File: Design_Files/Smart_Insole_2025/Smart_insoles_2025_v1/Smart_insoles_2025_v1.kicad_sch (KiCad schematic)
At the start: 9 parts, among them J1 Conn_01x20, U1 ESP32-C3_SUPERMINI_SMD, U2 CD74HC4067M96

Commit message: updated Schematic & PCB layout
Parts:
- added C2, C3: C, Capacitor_SMD:C_0603_1608Metric_Pad1.08x0.95mm_HandSolder, symbol Device:C
- added J2: Conn_01x02_Pin, Connector_JST:JST_EH_S2B-EH_1x02_P2.50mm_Horizontal, symbol Connector:Conn_01x02_Pin
- RN1, RN2: value R_Pack04 -> 10k
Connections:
- net +BATT: now also J2.2 (Pin_2)
- net -BATT: now also J2.1 (Pin_1)
- net GND: now also C2.2, C3.2
- net VCC: now also C2.1, C3.1
- no-connect marks 19 -> 20
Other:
- note added: "Decoupling Capacitors"
- note added: "MCU"

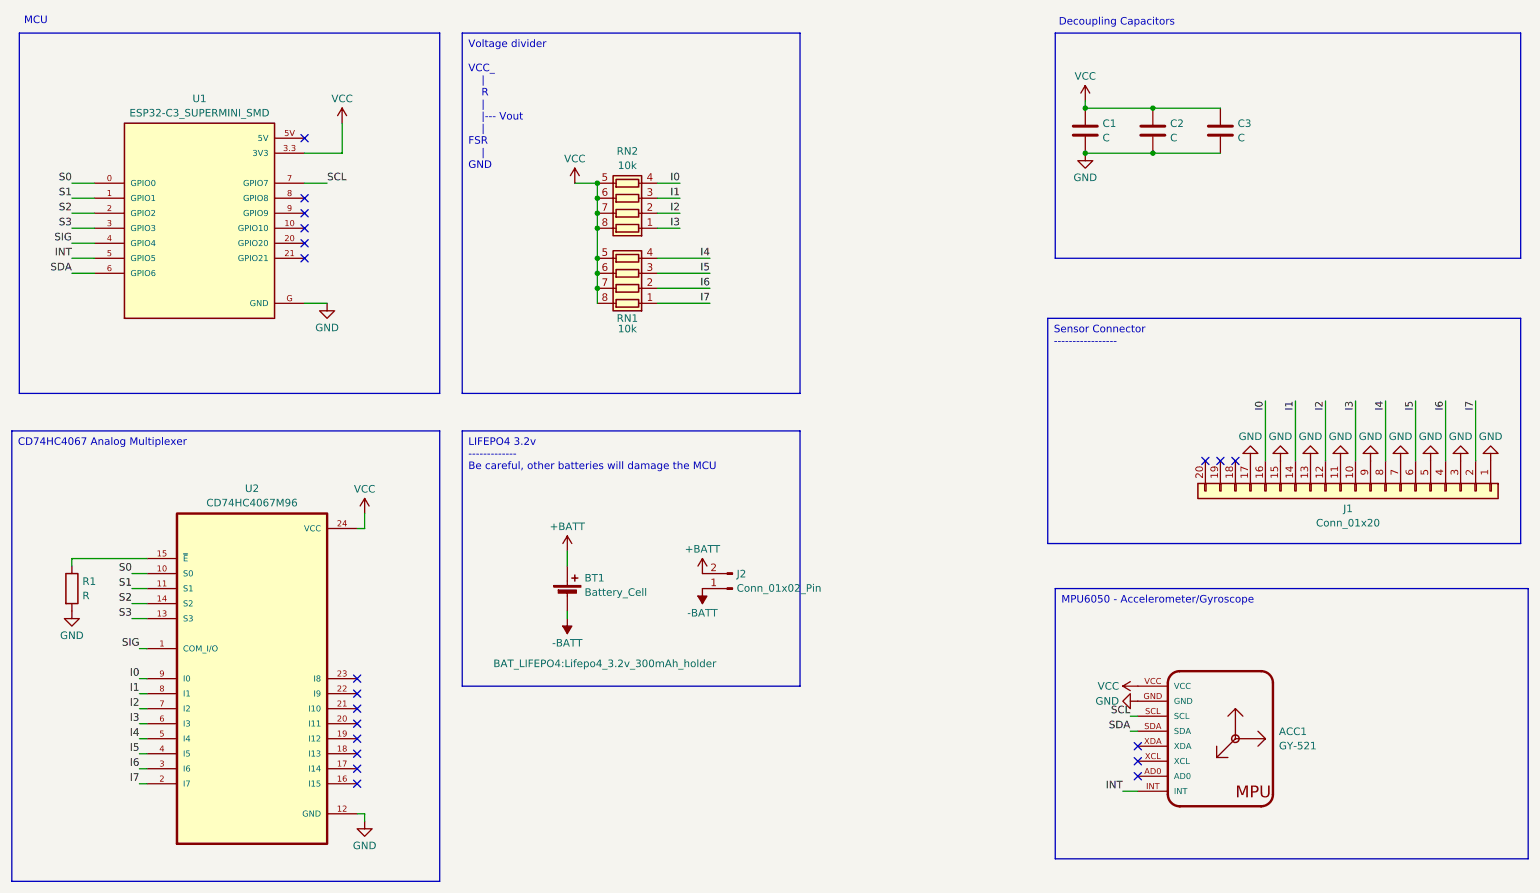
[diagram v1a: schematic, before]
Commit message: Added AFE from mikroe clicker schematic. Reorganized Schematic in general
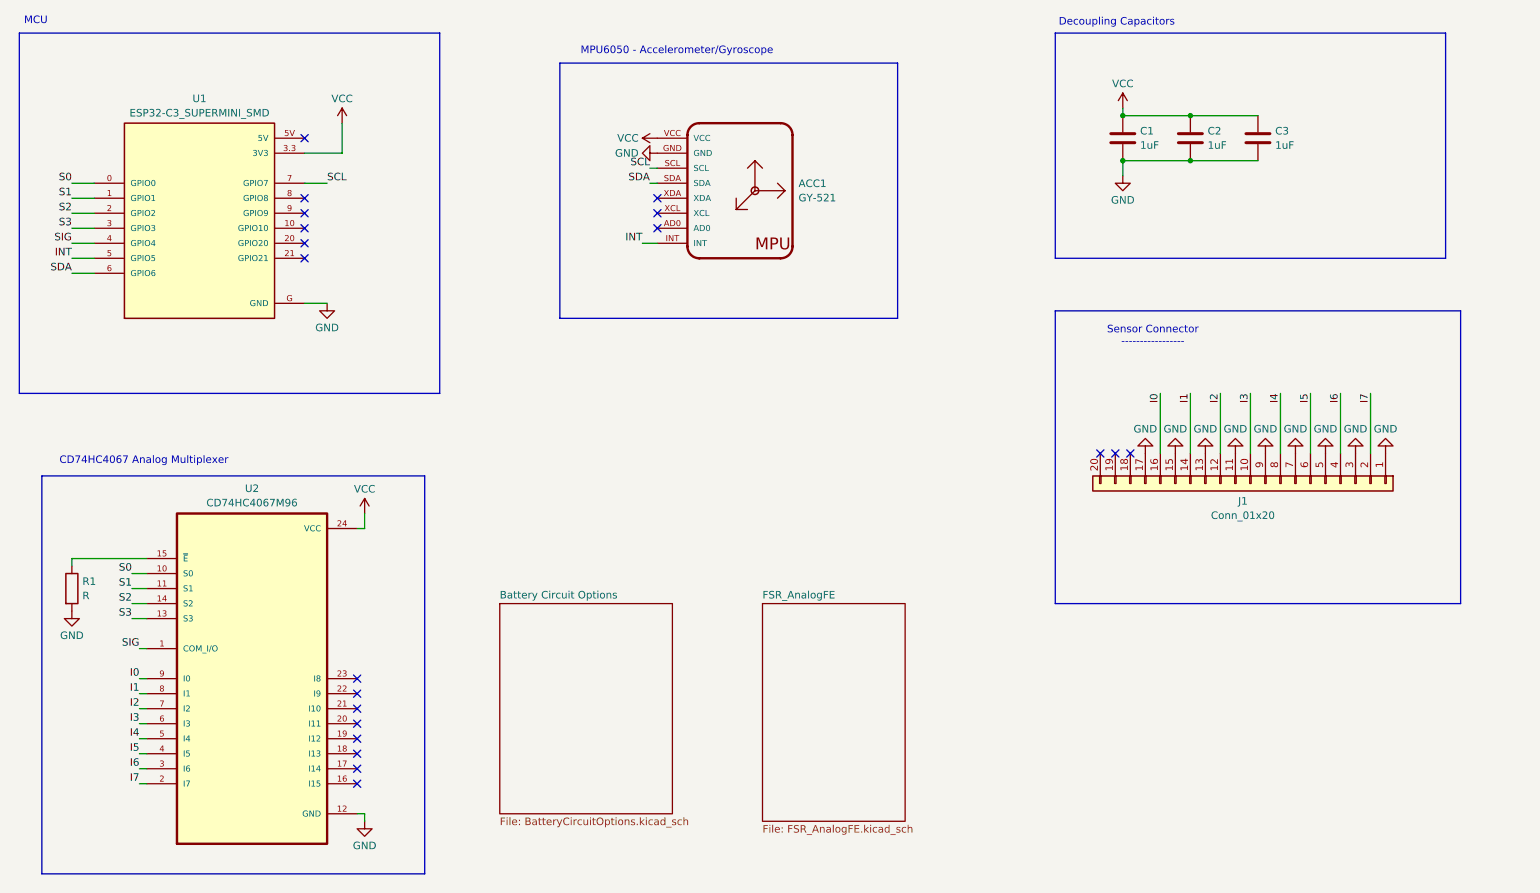
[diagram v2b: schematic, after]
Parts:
- removed BT1: Battery_Cell, BAT_LIFEPO4:Lifepo4_3.2v_300mAh_holder, symbol Device:Battery_Cell
- removed J2: Conn_01x02_Pin, Connector_JST:JST_EH_S2B-EH_1x02_P2.50mm_Horizontal, symbol Connector:Conn_01x02_Pin
- removed RN1, RN2: 10k, Resistor_SMD:R_Array_Concave_4x0603, symbol Device:R_Pack04
- C1, C2, C3: value C -> 1uF
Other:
- added sheet Battery Circuit Options (BatteryCircuitOptions.kicad_sch)
- added sheet FSR_AnalogFE (FSR_AnalogFE.kicad_sch)
- note added: "CD74HC4067 Analog Multiplexer"
- note added: "MPU6050 - Accelerometer/Gyroscope"
- note added: "Sensor Connector -----------------"
- moved on the sheet: ACC1, C1, C2, C3, J1

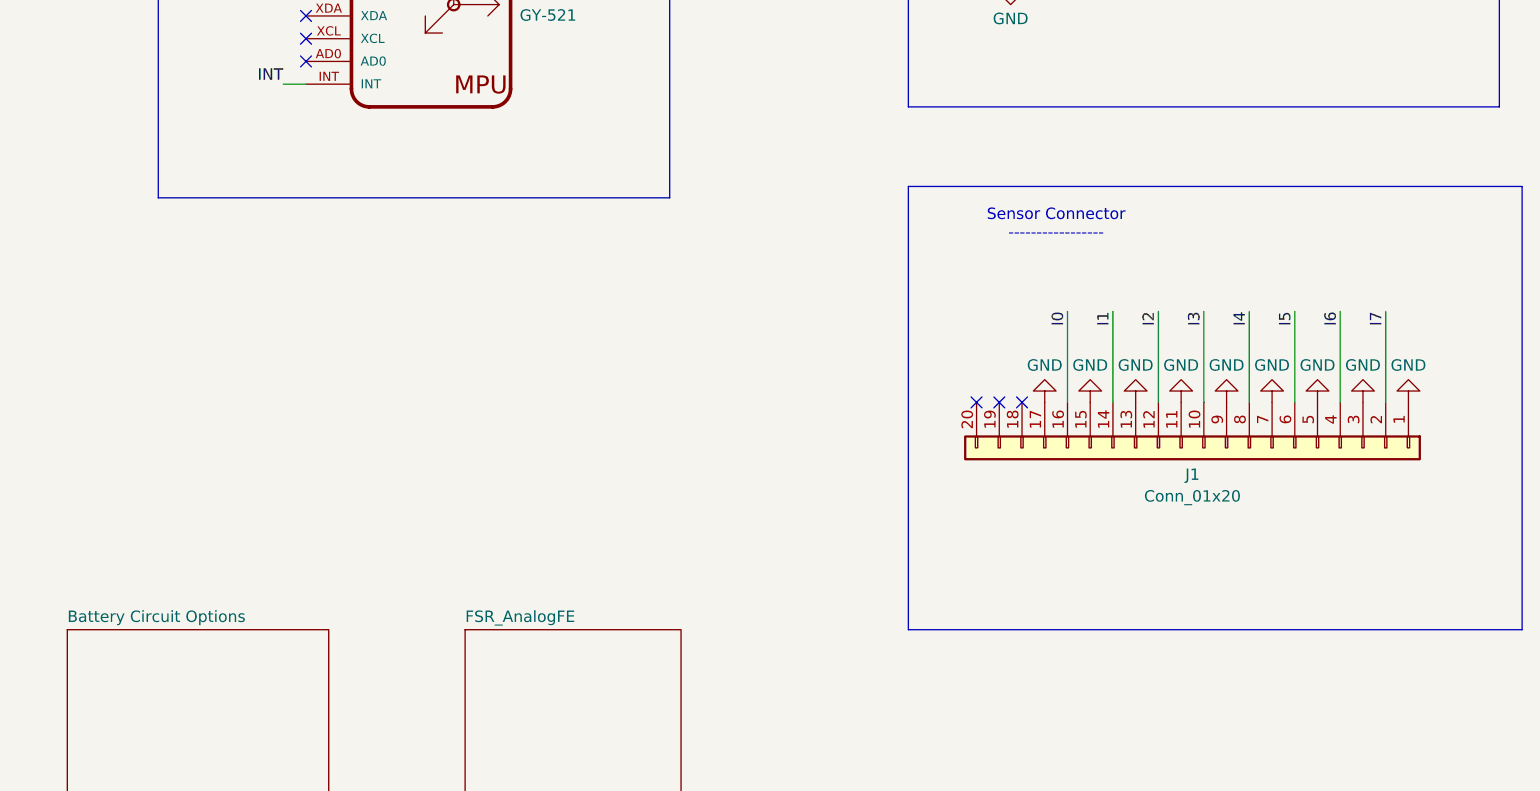
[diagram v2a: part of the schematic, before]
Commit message: Added different AFE circuits to the schematic. Needs verification
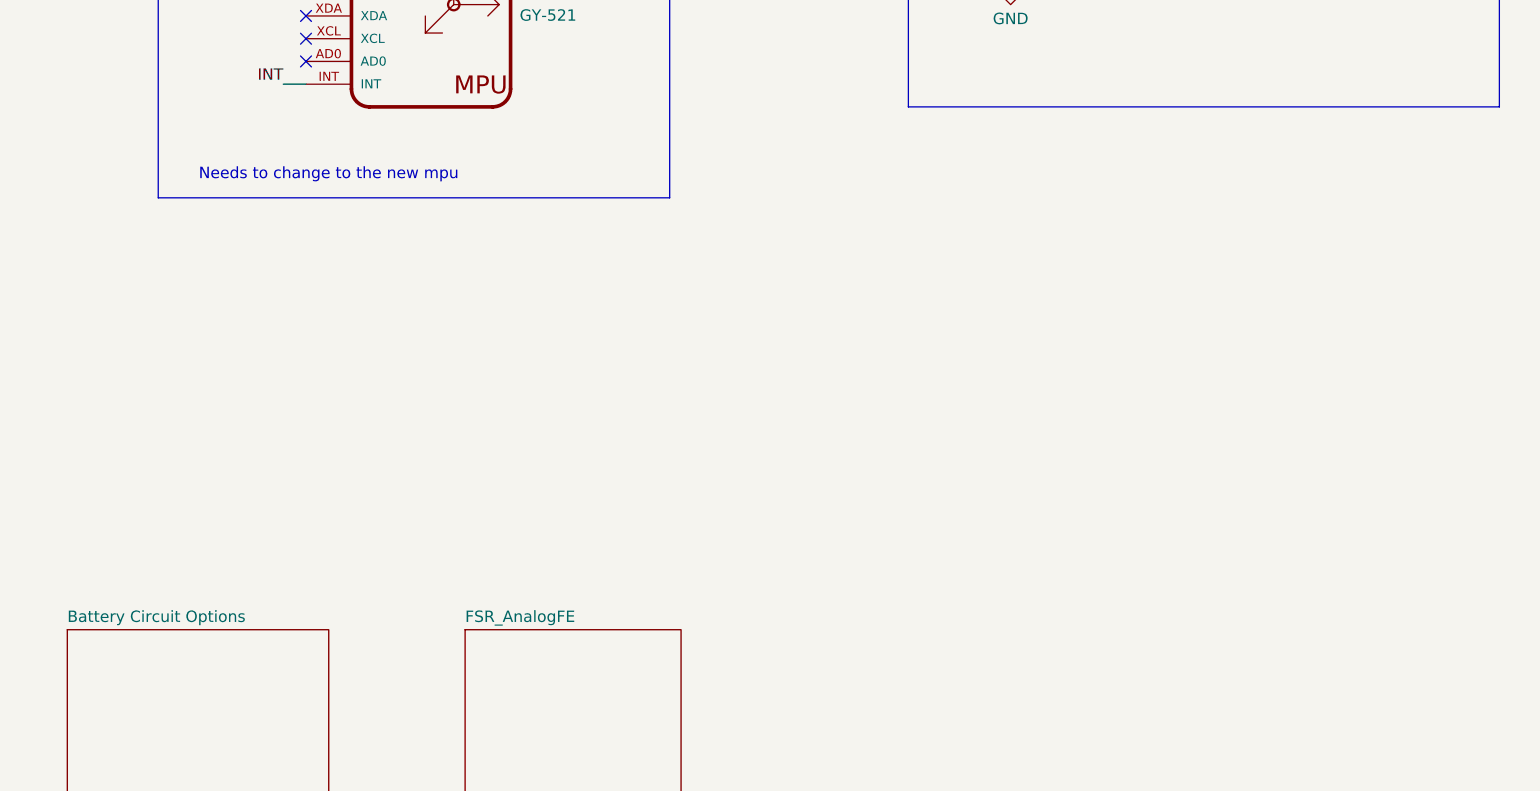
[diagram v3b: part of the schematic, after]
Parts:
- removed J1: Conn_01x20, Connector_Samtec_MicroMate:Samtec_T1M-20-X-S-RA_1x20-1MP_P1.0mm_Terminal_Horizontal, symbol Connector_Generic:Conn_01x20
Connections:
- no-connect marks 20 -> 17
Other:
- note added: "Needs to change to the new mpu"
- note removed: "Sensor Connector -----------------"

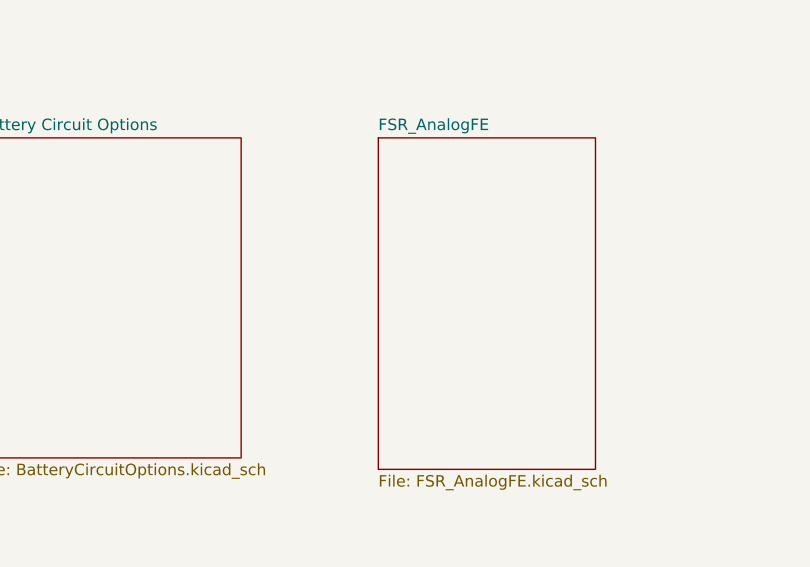
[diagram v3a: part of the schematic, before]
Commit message: added 3x3 trimpot symbol/footprint. Also Modify schematic to add 3x3trimpots
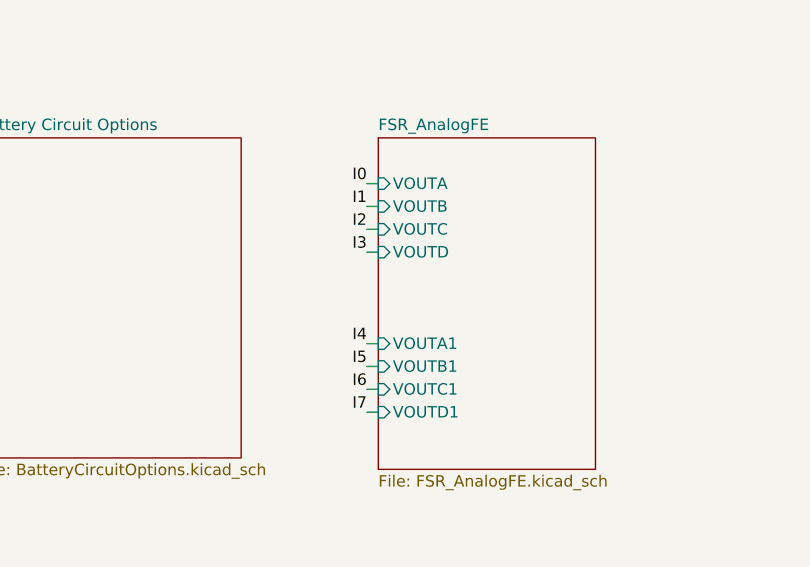
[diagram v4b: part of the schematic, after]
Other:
- sheet FSR_AnalogFE ports: added VOUTA, VOUTA1, VOUTB, VOUTB1, VOUTC, VOUTC1, VOUTD, VOUTD1; removed none
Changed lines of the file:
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@@
+	(wire
+		(pts
+			(xy 149.86 132.08) (xy 151.13 132.08)
+		)
+		(stroke
+			(width 0)
+			(type default)
+		)
+	)
 	(wire
 		(pts
@@
 	(wire
 		(pts
+			(xy 149.86 129.54) (xy 151.13 129.54)
+		)
+		(stroke
+			(width 0)
+			(type default)
+		)
+	)
+	(wire
+		(pts
 			(xy 46.99 111.76) (xy 34.29 111.76)
 		)
@@
 	(wire
 		(pts
+			(xy 149.86 124.46) (xy 151.13 124.46)
+		)
+		(stroke
+			(width 0)
+			(type default)
+		)
+	)
+	(wire
+		(pts
 			(xy 34.29 48.26) (xy 38.1 48.26)
 		)
@@
 	(wire
 		(pts
+			(xy 149.86 144.78) (xy 151.13 144.78)
+		)
+		(stroke
+			(width 0)
+			(type default)
+		)
+	)
+	(wire
+		(pts
+			(xy 149.86 147.32) (xy 151.13 147.32)
+		)
+		(stroke
+			(width 0)
+			(type default)
+		)
+	)
+	(wire
+		(pts
 			(xy 34.29 60.96) (xy 38.1 60.96)
 		)
@@
 	(wire
 		(pts
+			(xy 149.86 127) (xy 151.13 127)
+		)
+		(stroke
+			(width 0)
+			(type default)
+		)
+	)
+	(wire
+		(pts
 			(xy 44.45 114.3) (xy 46.99 114.3)
 		)
@@
 	(wire
 		(pts
+			(xy 149.86 149.86) (xy 151.13 149.86)
+		)
+		(stroke
+			(width 0)
+			(type default)
+		)
+	)
+	(wire
+		(pts
 			(xy 45.72 142.24) (xy 46.99 142.24)
 		)
@@
 		(pts
 			(xy 223.52 36.83) (xy 234.95 36.83)
+		)
+		(stroke
+			(width 0)
+			(type default)
+		)
+	)
+	(wire
+		(pts
+			(xy 149.86 142.24) (xy 151.13 142.24)
 		)
 		(stroke
@@
 		)
 	)
+	(label "I1"
+		(at 149.86 127 180)
+		(fields_autoplaced yes)
+		(effects
+			(font
+				(size 1.27 1.27)
+			)
+			(justify right bottom)
+		)
+	)
 	(label "S1"
 		(at 34.29 50.8 180)
@@
 		)
 	)
+	(label "I5"
+		(at 149.86 144.78 180)
+		(fields_autoplaced yes)
+		(effects
+			(font
+				(size 1.27 1.27)
+			)
+			(justify right bottom)
+		)
+	)
 	(label "I6"
 		(at 45.72 147.32 180)
@@
 		)
 	)
+	(label "I6"
+		(at 149.86 147.32 180)
+		(fields_autoplaced yes)
+		(effects
+			(font
+				(size 1.27 1.27)
+			)
+			(justify right bottom)
+		)
+	)
 	(label "S2"
 		(at 44.45 119.38 180)
@@
 	)
 	(label "I0"
+		(at 149.86 124.46 180)
+		(fields_autoplaced yes)
+		(effects
+			(font
+				(size 1.27 1.27)
+			)
+			(justify right bottom)
+		)
+	)
+	(label "I7"
+		(at 149.86 149.86 180)
+		(fields_autoplaced yes)
+		(effects
+			(font
+				(size 1.27 1.27)
+			)
+			(justify right bottom)
+		)
+	)
+	(label "I4"
+		(at 149.86 142.24 180)
+		(fields_autoplaced yes)
+		(effects
+			(font
+				(size 1.27 1.27)
+			)
+			(justify right bottom)
+		)
+	)
+	(label "I0"
 		(at 45.72 132.08 180)
 		(fields_autoplaced yes)
@@
 		)
 	)
+	(label "I2"
+		(at 149.86 129.54 180)
+		(fields_autoplaced yes)
+		(effects
+			(font
+				(size 1.27 1.27)
+			)
+			(justify right bottom)
+		)
+	)
 	(label "INT"
 		(at 130.81 58.42 180)
@@
 	(label "SIG"
 		(at 45.72 127 180)
+		(fields_autoplaced yes)
+		(effects
+			(font
+				(size 1.27 1.27)
+			)
+			(justify right bottom)
+		)
+	)
+	(label "I3"
+		(at 149.86 132.08 180)
 		(fields_autoplaced yes)
 		(effects
@@
 			)
 		)
+		(pin "VOUTD1" input
+			(at 151.13 149.86 180)
+			(effects
+				(font
+					(size 1.27 1.27)
+				)
+				(justify left)
+			)
+		)
+		(pin "VOUTC1" input
+			(at 151.13 147.32 180)
+			(effects
+				(font
+					(size 1.27 1.27)
+				)
+				(justify left)
+			)
+		)
+		(pin "VOUTA1" input
+			(at 151.13 142.24 180)
+			(effects
+				(font
+					(size 1.27 1.27)
+				)
+				(justify left)
+			)
+		)
+		(pin "VOUTB1" input
+			(at 151.13 144.78 180)
+			(effects
+				(font
+					(size 1.27 1.27)
+				)
+				(justify left)
+			)
+		)
+		(pin "VOUTA" input
+			(at 151.13 124.46 180)
+			(effects
+				(font
+					(size 1.27 1.27)
+				)
+				(justify left)
+			)
+		)
+		(pin "VOUTD" input
+			(at 151.13 132.08 180)
+			(effects
+				(font
+					(size 1.27 1.27)
+				)
+				(justify left)
+			)
+		)
+		(pin "VOUTC" input
+			(at 151.13 129.54 180)
+			(effects
+				(font
+					(size 1.27 1.27)
+				)
+				(justify left)
+			)
+		)
+		(pin "VOUTB" input
+			(at 151.13 127 180)
+			(effects
+				(font
+					(size 1.27 1.27)
+				)
+				(justify left)
+			)
+		)

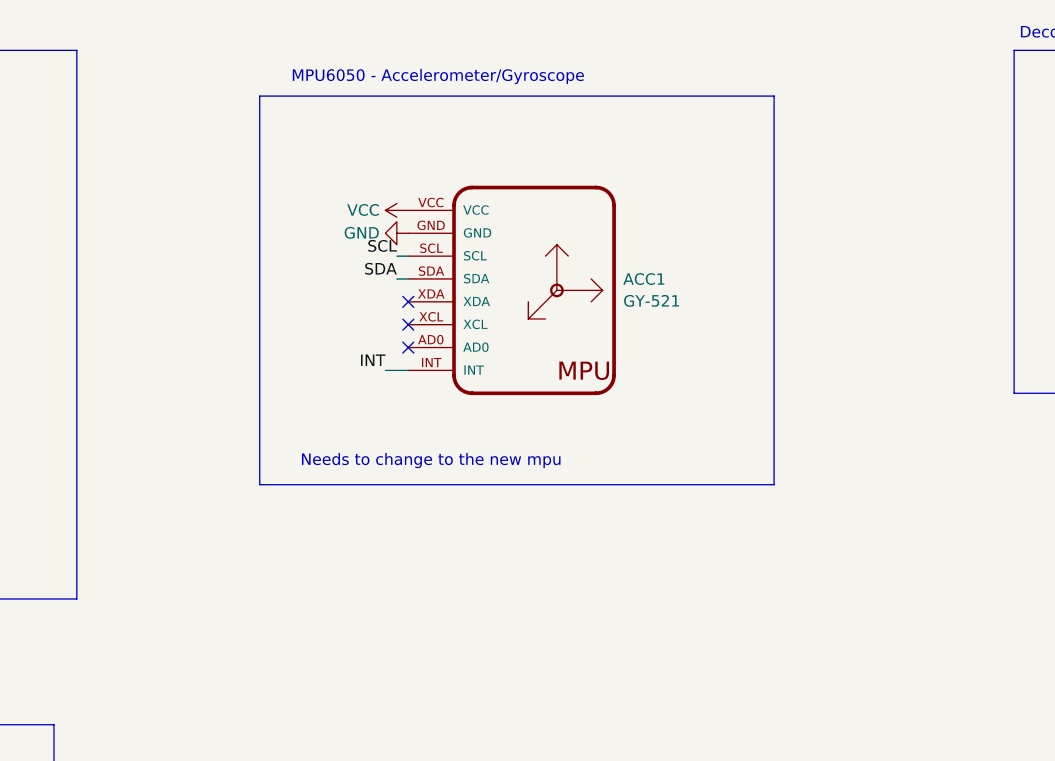
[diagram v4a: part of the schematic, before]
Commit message: Change accelerometer to Lsm6ds033
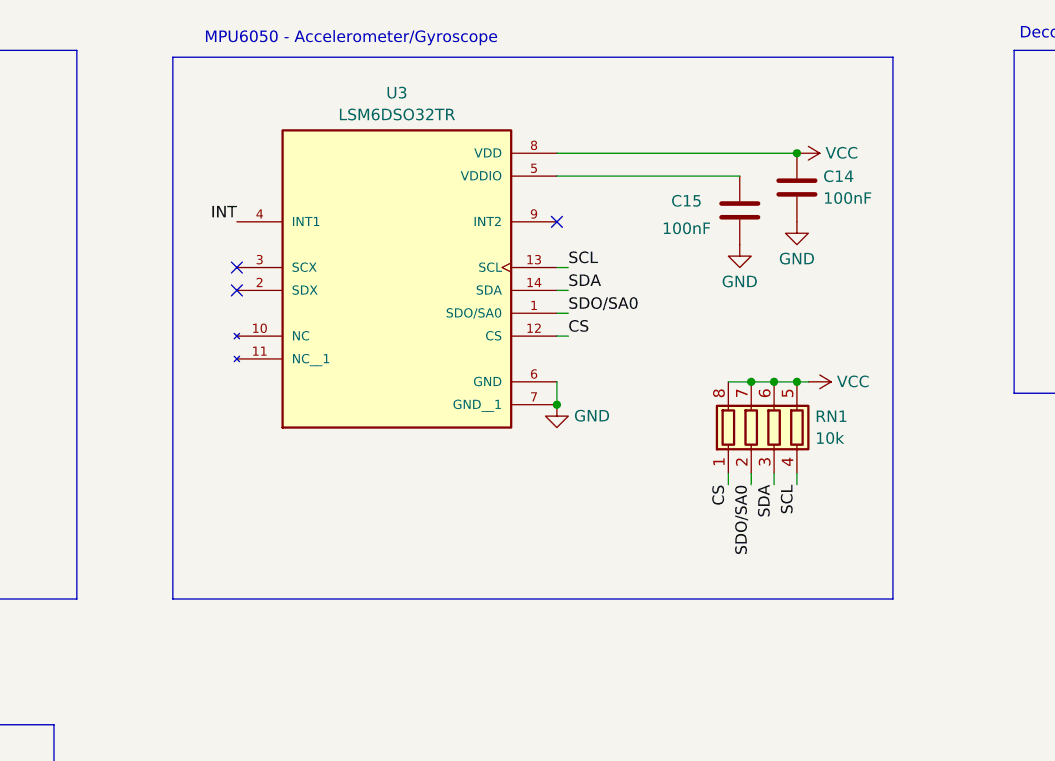
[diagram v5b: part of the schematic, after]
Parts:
- removed ACC1: GY-521, GY-521:GY-521_SMD, symbol GY-521:GY-521
- added C14, C15: 100nF, Capacitor_SMD:C_0603_1608Metric_Pad1.08x0.95mm_HandSolder, symbol Device:C
- added RN1: 10k, Resistor_SMD:R_Array_Concave_4x0603, symbol Device:R_Pack04
- added U3: LSM6DSO32TR, LSM6DSO32TR:XDCR_LSM6DSO32TR, symbol LSM6DSO32TR:LSM6DSO32TR
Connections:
- net GND: now also C14.2, C15.2, U3.6 (GND), U3.7 (GND__1)
- net INT: now also U3.4 (INT1)
- net SCL: now also RN1.4 (R4.1), U3.13 (SCL)
- net SDA: now also RN1.3 (R3.1), U3.14 (SDA)
- net VCC: now also C14.1, RN1.5 (R4.2), RN1.6 (R3.2), RN1.7 (R2.2), RN1.8 (R1.2), U3.8 (VDD)
- new net: C15.1, U3.5 (VDDIO)
- new net CS: RN1.1 (R1.1), U3.12 (CS)
- new net SDO/SA0: RN1.2 (R2.1), U3.1 (SDO/SA0)
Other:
- note removed: "Needs to change to the new mpu"
